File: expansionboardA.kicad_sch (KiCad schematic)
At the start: 52 parts, among them J1 DEBUG, J2 USB_A_Stacked, J3 HDMI_A, J4 FAN, P1 USB_C_Plug, U1 MAX3420EECJ, U2 GPIO_U2, U3 AMS1117-3.3, U4 GPIO_U4, U5 MCP3008T-I/SL, U6 CS4344-CZZR, Y1 Crystal

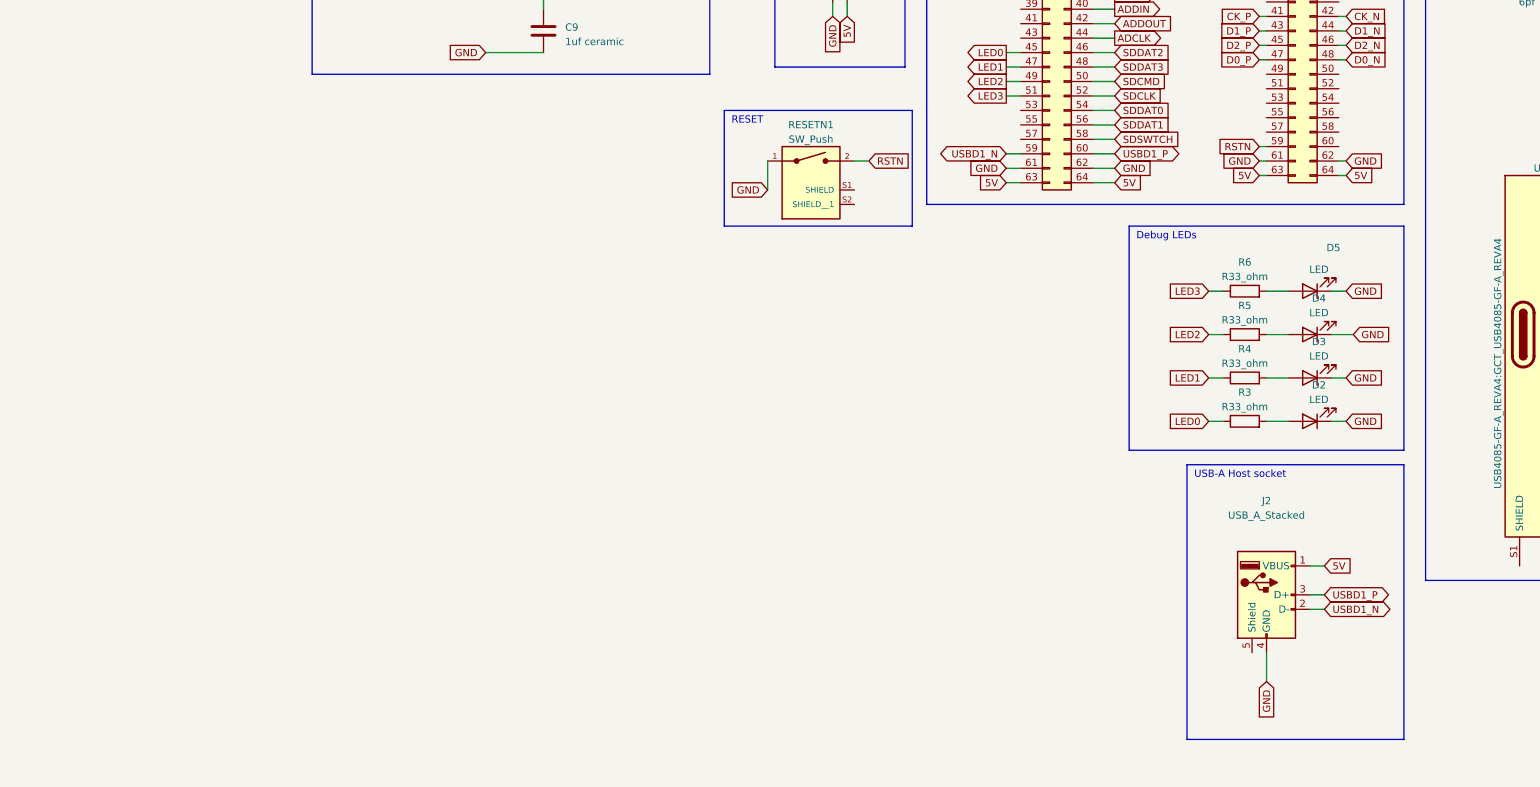
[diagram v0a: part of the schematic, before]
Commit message: Adding USB host chip
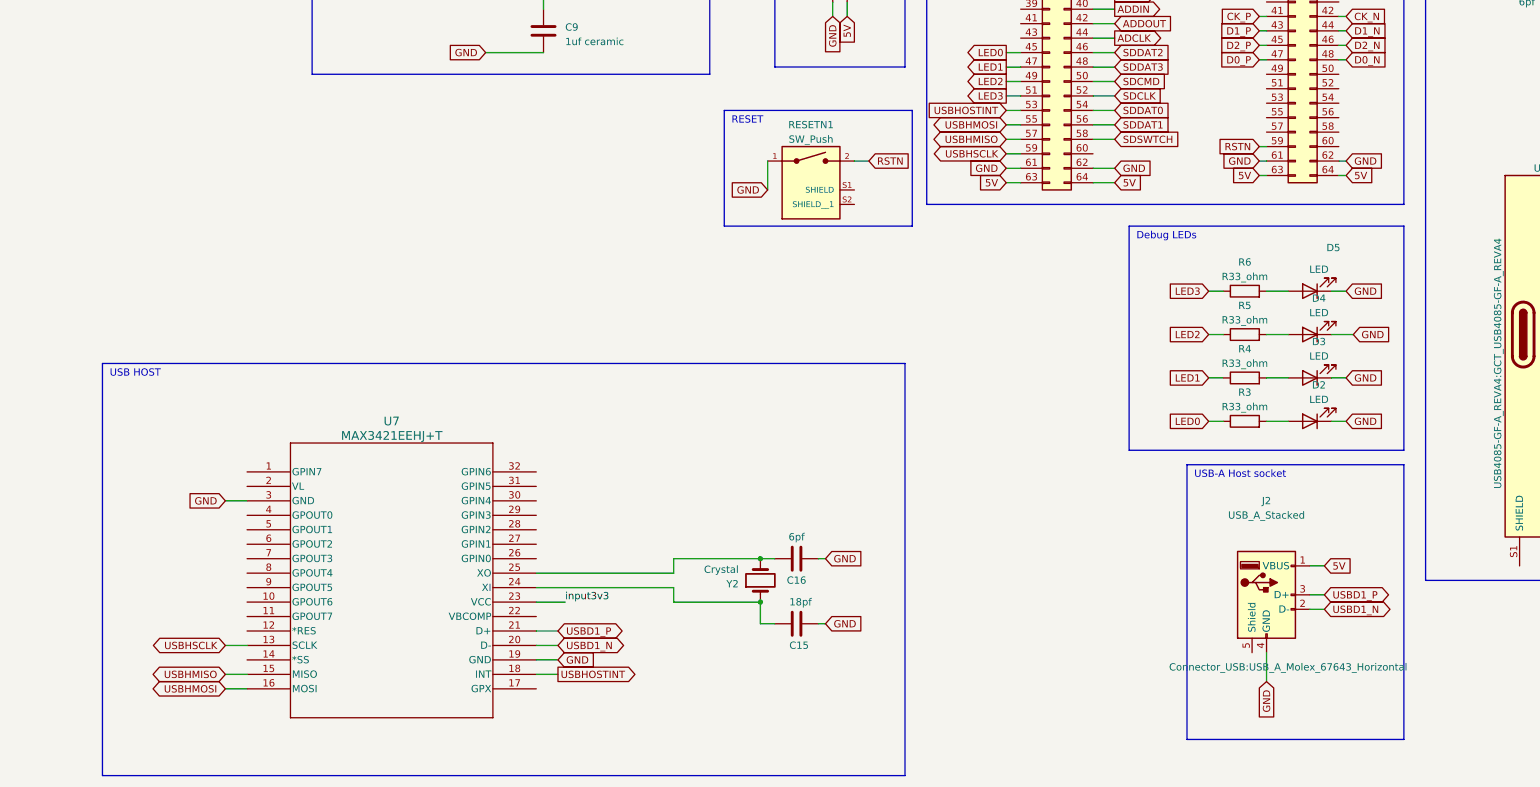
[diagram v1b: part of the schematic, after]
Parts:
- added C15: 18pf, Capacitor_SMD:C_0603_1608Metric_Pad1.08x0.95mm_HandSolder, symbol Device:C
- added C16: 6pf, Capacitor_SMD:C_0603_1608Metric_Pad1.08x0.95mm_HandSolder, symbol Device:C
- added U7: MAX3421EEHJ+T, 21-0110-C_90-0149-32L_MXM, symbol 2023-04-30_01-05-07:MAX3421EEHJ+T
- added Y2: Crystal, Crystal:Crystal_AT310_D3.0mm_L10.0mm_Horizontal, symbol Device:Crystal
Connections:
- net GND: now also C15.1, C16.1, U7.19 (GND), U7.3 (GND)
- net USBD1_N: now also U7.20 (D-); no longer U2.59 (Pin_59)
- net USBD1_P: now also U7.21 (D+); no longer U2.60 (Pin_60)
- net input3v3: now also U7.23 (VCC)
- net USBHOSTINT: now reaches U2.53 (Pin_53)
- net USBHOSTINT: now also U7.18 (INT)
- net USBHMOSI: now reaches U2.55 (Pin_55)
- net USBHMOSI: now also U7.16 (MOSI)
- net USBHMISO: now reaches U2.57 (Pin_57)
- net USBHMISO: now also U7.15 (MISO)
- new net: C15.2, U7.24 (XI), Y2.1
- new net: C16.2, U7.25 (XO), Y2.2
- new net USBHSCLK: U2.59 (Pin_59), U7.13 (SCLK)
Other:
- note added: "USB HOST"

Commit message: Updated board
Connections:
- net USBGPIN0: no longer names the net of U2.21 (Pin_21)
- net USBGPIN0: no longer U1.29 (GPIN0)
- net USBGPIN1: no longer names the net of U2.22 (Pin_22)
- net USBGPIN1: no longer U1.30 (GPIN1)
- net USBGPIN2: no longer names the net of U2.19 (Pin_19)
- net USBGPIN2: no longer U1.31 (GPIN2)
- net USBGPIN3: no longer names the net of U2.20 (Pin_20)
- net USBGPIN3: no longer U1.32 (GPIN3)
- net USBGPOUT0: no longer names the net of U2.17 (Pin_17)
- net USBGPOUT0: no longer U1.1 (GPOUT0)
- net USBGPOUT1: no longer names the net of U2.18 (Pin_18)
- net USBGPOUT1: no longer U1.2 (GPOUT1)
- net USBGPOUT2: no longer names the net of U2.15 (Pin_15)
- net USBGPOUT2: no longer U1.7 (GPOUT2)
- net USBGPOUT3: no longer names the net of U2.16 (Pin_16)
- net USBGPOUT3: no longer U1.8 (GPOUT3)
- net USBHOSTINT renamed USBHINT
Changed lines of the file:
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@@
-    (stroke (width 0) (type default))
-  )
-  (wire (pts (xy 322.58 106.68) (xy 323.85 106.68))
     (stroke (width 0) (type default))
   )
@@
     (stroke (width 0) (type default))
   )
-  (wire (pts (xy 322.58 111.76) (xy 323.85 111.76))
-    (stroke (width 0) (type default))
-  )
   (wire (pts (xy 133.35 109.22) (xy 130.81 109.22))
     (stroke (width 0) (type default))
@@
     (stroke (width 0) (type default))
   )
-  (wire (pts (xy 359.41 106.68) (xy 361.95 106.68))
-    (stroke (width 0) (type default))
-  )
   (wire (pts (xy 378.46 86.36) (xy 378.46 95.25))
     (stroke (width 0) (type default))
@@
     (stroke (width 0) (type default))
   )
-  (wire (pts (xy 322.58 104.14) (xy 323.85 104.14))
-    (stroke (width 0) (type default))
-  )
   (wire (pts (xy 133.35 119.38) (xy 130.81 119.38))
     (stroke (width 0) (type default))
@@
     (stroke (width 0) (type default))
   )
-  (wire (pts (xy 359.41 109.22) (xy 361.95 109.22))
-    (stroke (width 0) (type default))
-  )
   (wire (pts (xy 96.52 25.4) (xy 100.33 25.4))
     (stroke (width 0) (type default))
@@
     (stroke (width 0) (type default))
   )
-  (wire (pts (xy 359.41 104.14) (xy 361.95 104.14))
-    (stroke (width 0) (type default))
-  )
   (wire (pts (xy 379.73 35.56) (xy 387.35 35.56))
     (stroke (width 0) (type default))
@@
     (stroke (width 0) (type default))
   )
-  (wire (pts (xy 359.41 111.76) (xy 361.95 111.76))
-    (stroke (width 0) (type default))
-  )
   (wire (pts (xy 219.71 147.32) (xy 215.9 147.32))
     (stroke (width 0) (type default))
@@
     (stroke (width 0) (type default))
   )
-  (wire (pts (xy 322.58 109.22) (xy 323.85 109.22))
-    (stroke (width 0) (type default))
-  )
   (wire (pts (xy 123.19 109.22) (xy 119.38 109.22))
     (stroke (width 0) (type default))
@@
     (effects (font (size 1.27 1.27)) (justify left bottom))
   )
-  (global_label "USBGPOUT2" (shape input) (at 201.93 96.52 180) (fields_autoplaced)
-    (effects (font (size 1.27 1.27)) (justify right))
-    (property "Intersheetrefs" "${INTERSHEET_REFS}" (at 187.8361 96.52 0)
-      (effects (font (size 1.27 1.27)) (justify right) hide)
-    )
-  )
   (global_label "GND" (shape input) (at 95.25 57.15 180) (fields_autoplaced)
     (effects (font (size 1.27 1.27)) (justify right))
@@
     )
   )
-  (global_label "USBGPOUT0" (shape input) (at 201.93 99.06 180) (fields_autoplaced)
-    (effects (font (size 1.27 1.27)) (justify right))
-    (property "Intersheetrefs" "${INTERSHEET_REFS}" (at 187.8361 99.06 0)
-      (effects (font (size 1.27 1.27)) (justify right) hide)
-    )
-  )
   (global_label "ADCS" (shape output) (at 219.71 124.46 0) (fields_autoplaced)
     (effects (font (size 1.27 1.27)) (justify left))
@@
     )
   )
-  (global_label "USBHOSTINT" (shape input) (at 200.66 144.78 180) (fields_autoplaced)
-    (effects (font (size 1.27 1.27)) (justify right))
-    (property "Intersheetrefs" "${INTERSHEET_REFS}" (at 186.2032 144.78 0)
-      (effects (font (size 1.27 1.27)) (justify right) hide)
-    )
-  )
-  (global_label "USBGPOUT3" (shape output) (at 361.95 111.76 0) (fields_autoplaced)
-    (effects (font (size 1.27 1.27)) (justify left))
-    (property "Intersheetrefs" "${INTERSHEET_REFS}" (at 376.0439 111.76 0)
-      (effects (font (size 1.27 1.27)) (justify left) hide)
-    )
-  )
-  (global_label "USBGPOUT1" (shape output) (at 361.95 106.68 0) (fields_autoplaced)
-    (effects (font (size 1.27 1.27)) (justify left))
-    (property "Intersheetrefs" "${INTERSHEET_REFS}" (at 376.0439 106.68 0)
-      (effects (font (size 1.27 1.27)) (justify left) hide)
+  (global_label "USBHINT" (shape input) (at 200.66 144.78 180) (fields_autoplaced)
+    (effects (font (size 1.27 1.27)) (justify right))
+    (property "Intersheetrefs" "${INTERSHEET_REFS}" (at 189.7108 144.78 0)
+      (effects (font (size 1.27 1.27)) (justify right) hide)
     )
   )
@@
     )
   )
-  (global_label "USBHOSTINT" (shape output) (at 121.92 243.84 0) (fields_autoplaced)
-    (effects (font (size 1.27 1.27)) (justify left))
-    (property "Intersheetrefs" "${INTERSHEET_REFS}" (at 136.3768 243.84 0)
+  (global_label "USBHINT" (shape output) (at 121.92 243.84 0) (fields_autoplaced)
+    (effects (font (size 1.27 1.27)) (justify left))
+    (property "Intersheetrefs" "${INTERSHEET_REFS}" (at 132.8692 243.84 0)
       (effects (font (size 1.27 1.27)) (justify left) hide)
     )
@@
     )
   )
-  (global_label "USBGPIN3" (shape input) (at 322.58 111.76 180) (fields_autoplaced)
-    (effects (font (size 1.27 1.27)) (justify right))
-    (property "Intersheetrefs" "${INTERSHEET_REFS}" (at 310.1794 111.76 0)
-      (effects (font (size 1.27 1.27)) (justify right) hide)
-    )
-  )
   (global_label "D2_P" (shape input) (at 30.48 34.29 180) (fields_autoplaced)
     (effects (font (size 1.27 1.27)) (justify right))
@@
     )
   )
-  (global_label "USBGPOUT3" (shape input) (at 217.17 96.52 0) (fields_autoplaced)
-    (effects (font (size 1.27 1.27)) (justify left))
-    (property "Intersheetrefs" "${INTERSHEET_REFS}" (at 231.2639 96.52 0)
-      (effects (font (size 1.27 1.27)) (justify left) hide)
-    )
-  )
   (global_label "GND" (shape input) (at 287.02 121.92 180) (fields_autoplaced)
     (effects (font (size 1.27 1.27)) (justify right))
@@
     )
   )
-  (global_label "USBGPIN3" (shape output) (at 217.17 101.6 0) (fields_autoplaced)
-    (effects (font (size 1.27 1.27)) (justify left))
-    (property "Intersheetrefs" "${INTERSHEET_REFS}" (at 229.5706 101.6 0)
-      (effects (font (size 1.27 1.27)) (justify left) hide)
-    )
-  )
   (global_label "GND" (shape input) (at 201.93 83.82 180) (fields_autoplaced)
     (effects (font (size 1.27 1.27)) (justify right))
@@
     )
   )
-  (global_label "USBGPIN0" (shape input) (at 322.58 104.14 180) (fields_autoplaced)
-    (effects (font (size 1.27 1.27)) (justify right))
-    (property "Intersheetrefs" "${INTERSHEET_REFS}" (at 310.1794 104.14 0)
-      (effects (font (size 1.27 1.27)) (justify right) hide)
-    )
-  )
   (global_label "USBD1_P" (shape bidirectional) (at 256.54 229.87 0) (fields_autoplaced)
     (effects (font (size 1.27 1.27)) (justify left))
@@
     )
   )
-  (global_label "USBGPIN2" (shape output) (at 200.66 101.6 180) (fields_autoplaced)
-    (effects (font (size 1.27 1.27)) (justify right))
-    (property "Intersheetrefs" "${INTERSHEET_REFS}" (at 188.2594 101.6 0)
-      (effects (font (size 1.27 1.27)) (justify right) hide)
-    )
-  )
   (global_label "ADCH3" (shape input) (at 129.54 83.82 270) (fields_autoplaced)
     (effects (font (size 1.27 1.27)) (justify right))
@@
     )
   )
-  (global_label "USBGPIN2" (shape input) (at 322.58 109.22 180) (fields_autoplaced)
-    (effects (font (size 1.27 1.27)) (justify right))
-    (property "Intersheetrefs" "${INTERSHEET_REFS}" (at 310.1794 109.22 0)
-      (effects (font (size 1.27 1.27)) (justify right) hide)
-    )
-  )
-  (global_label "USBGPIN1" (shape input) (at 322.58 106.68 180) (fields_autoplaced)
-    (effects (font (size 1.27 1.27)) (justify right))
-    (property "Intersheetrefs" "${INTERSHEET_REFS}" (at 310.1794 106.68 0)
-      (effects (font (size 1.27 1.27)) (justify right) hide)
-    )
-  )
-  (global_label "USBGPOUT0" (shape output) (at 361.95 104.14 0) (fields_autoplaced)
-    (effects (font (size 1.27 1.27)) (justify left))
-    (property "Intersheetrefs" "${INTERSHEET_REFS}" (at 376.0439 104.14 0)
-      (effects (font (size 1.27 1.27)) (justify left) hide)
-    )
-  )
   (global_label "GND" (shape input) (at 260.35 82.55 0) (fields_autoplaced)
     (effects (font (size 1.27 1.27)) (justify left))
@@
     )
   )
-  (global_label "USBGPOUT2" (shape output) (at 361.95 109.22 0) (fields_autoplaced)
-    (effects (font (size 1.27 1.27)) (justify left))
-    (property "Intersheetrefs" "${INTERSHEET_REFS}" (at 376.0439 109.22 0)
-      (effects (font (size 1.27 1.27)) (justify left) hide)
-    )
-  )
   (global_label "CK_P" (shape input) (at 30.48 49.53 180) (fields_autoplaced)
     (effects (font (size 1.27 1.27)) (justify right))
@@
     )
   )
-  (global_label "USBGPIN1" (shape output) (at 217.17 104.14 0) (fields_autoplaced)
-    (effects (font (size 1.27 1.27)) (justify left))
-    (property "Intersheetrefs" "${INTERSHEET_REFS}" (at 229.5706 104.14 0)
-      (effects (font (size 1.27 1.27)) (justify left) hide)
-    )
-  )
   (global_label "GND" (shape input) (at 177.8 53.34 180) (fields_autoplaced)
     (effects (font (size 1.27 1.27)) (justify right))
@@
     )
   )
-  (global_label "USBGPIN0" (shape output) (at 200.66 104.14 180) (fields_autoplaced)
-    (effects (font (size 1.27 1.27)) (justify right))
-    (property "Intersheetrefs" "${INTERSHEET_REFS}" (at 188.2594 104.14 0)
-      (effects (font (size 1.27 1.27)) (justify right) hide)
-    )
-  )
   (global_label "SDDAT0" (shape input) (at 177.8 27.94 180) (fields_autoplaced)
     (effects (font (size 1.27 1.27)) (justify right))
@@
     )
   )
-  (global_label "USBGPX" (shape input) (at 361.95 91.44 0) (fields_autoplaced)
+  (global_label "USBGPX" (shape output) (at 361.95 91.44 0) (fields_autoplaced)
     (effects (font (size 1.27 1.27)) (justify left))
     (property "Intersheetrefs" "${INTERSHEET_REFS}" (at 372.4153 91.44 0)
@@
     )
   )
-  (global_label "USBGPOUT1" (shape input) (at 217.17 99.06 0) (fields_autoplaced)
-    (effects (font (size 1.27 1.27)) (justify left))
-    (property "Intersheetrefs" "${INTERSHEET_REFS}" (at 231.2639 99.06 0)
-      (effects (font (size 1.27 1.27)) (justify left) hide)
-    )
-  )

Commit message: Fixed some errors on the board
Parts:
- added R15: 10_kohm, Resistor_SMD:R_0603_1608Metric_Pad0.98x0.95mm_HandSolder, symbol Device:R
- C4: value 6pf -> 18pf
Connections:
- net INT: now also R15.1
- net input3v3: now also R15.2
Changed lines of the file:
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@@
   (junction (at 359.41 57.15) (diameter 0) (color 0 0 0 0)
   )
+  (junction (at 375.92 86.36) (diameter 0) (color 0 0 0 0)
+  )
   (junction (at 241.3 39.37) (diameter 0) (color 0 0 0 0)
   )
@@
   (junction (at 119.38 119.38) (diameter 0) (color 0 0 0 0)
   )
+  (junction (at 360.68 93.98) (diameter 0) (color 0 0 0 0)
+  )
   (junction (at 307.34 96.52) (diameter 0) (color 0 0 0 0)
   )
@@
     (stroke (width 0) (type default))
   )
+  (wire (pts (xy 360.68 93.98) (xy 361.95 93.98))
+    (stroke (width 0) (type default))
+  )
   (wire (pts (xy 171.45 25.4) (xy 182.88 25.4))
     (stroke (width 0) (type default))
@@
     (stroke (width 0) (type default))
   )
-  (wire (pts (xy 361.95 86.36) (xy 378.46 86.36))
+  (wire (pts (xy 375.92 101.6) (xy 375.92 86.36))
+    (stroke (width 0) (type default))
+  )
+  (wire (pts (xy 361.95 86.36) (xy 375.92 86.36))
     (stroke (width 0) (type default))
   )
@@
     (stroke (width 0) (type default))
   )
-  (wire (pts (xy 359.41 93.98) (xy 361.95 93.98))
+  (wire (pts (xy 359.41 93.98) (xy 360.68 93.98))
     (stroke (width 0) (type default))
   )
@@
     (stroke (width 0) (type default))
   )
+  (wire (pts (xy 360.68 93.98) (xy 360.68 101.6))
+    (stroke (width 0) (type default))
+  )
   (wire (pts (xy 246.38 130.81) (xy 245.11 130.81))
     (stroke (width 0) (type default))
@@
     (stroke (width 0) (type default))
   )
+  (wire (pts (xy 360.68 101.6) (xy 363.22 101.6))
+    (stroke (width 0) (type default))
+  )
   (wire (pts (xy 219.71 127) (xy 215.9 127))
     (stroke (width 0) (type default))
@@
     (stroke (width 0) (type default))
   )
+  (wire (pts (xy 370.84 101.6) (xy 375.92 101.6))
+    (stroke (width 0) (type default))
+  )
   (wire (pts (xy 302.26 224.79) (xy 298.45 224.79))
     (stroke (width 0) (type default))
@@
     (stroke (width 0) (type default))
   )
+  (wire (pts (xy 375.92 86.36) (xy 378.46 86.36))
+    (stroke (width 0) (type default))
+  )
   (wire (pts (xy 287.02 121.92) (xy 288.29 121.92))
     (stroke (width 0) (type default))
@@
     )
   )
+  (symbol (lib_id "Device:R") (at 367.03 101.6 90) (unit 1)
+    (in_bom yes) (on_board yes) (dnp no) (fields_autoplaced)
+    (property "Reference" "R15" (at 367.03 96.52 90)
+      (effects (font (size 1.27 1.27)))
+    )
+    (property "Value" "10_kohm" (at 367.03 99.06 90)
+      (effects (font (size 1.27 1.27)))
+    )
+    (property "Footprint" "Resistor_SMD:R_0603_1608Metric_Pad0.98x0.95mm_HandSolder" (at 367.03 103.378 90)
+      (effects (font (size 1.27 1.27)) hide)
+    )
+    (property "Datasheet" "~" (at 367.03 101.6 0)
+      (effects (font (size 1.27 1.27)) hide)
+    )
+    (pin "1")
+    (pin "2")
+    (instances
+      (project "expansionboardA"
+        (path "/317f7f3e-4535-46d0-9a87-af1bea12706a"
+          (reference "R15") (unit 1)
+        )
+      )
+    )
+  )
   (symbol (lib_id "Connector_Generic:Conn_01x02") (at 170.18 120.65 90) (unit 1)
     (in_bom yes) (on_board yes) (dnp no)
@@
       (effects (font (size 1.27 1.27)))
     )
-    (property "Value" "6pf" (at 292.1 125.73 90)
+    (property "Value" "18pf" (at 292.1 125.73 90)
       (effects (font (size 1.27 1.27)))
     )

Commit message: Updated board
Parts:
- removed R15: 10_kohm, Resistor_SMD:R_0603_1608Metric_Pad0.98x0.95mm_HandSolder, symbol Device:R
- added C17: 1uf ceramic, Capacitor_SMD:C_0603_1608Metric_Pad1.08x0.95mm_HandSolder, symbol Device:C
- added C18: 0.1uf, Capacitor_SMD:C_0603_1608Metric_Pad1.08x0.95mm_HandSolder, symbol Device:C
- added C20: 4.7uf, Capacitor_THT:CP_Radial_D4.0mm_P1.50mm, symbol Device:C_Polarized_Small_US
- added R16, R17: R33_ohm, Resistor_SMD:R_0603_1608Metric_Pad0.98x0.95mm_HandSolder, symbol Device:R
- added R18: 10_kohm, Resistor_SMD:R_0603_1608Metric_Pad0.98x0.95mm_HandSolder, symbol Device:R
- C16: value 6pf -> 18pf
- C5: value 1uf ceramic -> 4.7uf; footprint Capacitor_SMD:C_0603_1608Metric_Pad1.08x0.95mm_HandSolder -> Capacitor_THT:CP_Radial_D4.0mm_P1.50mm; symbol Device:C -> Device:C_Polarized_Small_US
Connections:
- net 5V: now also C20.1
- net GND: now also C5.2, J2.5 (Shield), C17.1, C18.1, C20.2; no longer C5.1
- net LED0: now also U2.43 (Pin_43); no longer U2.45 (Pin_45)
- net LED1: now also U2.45 (Pin_45); no longer U2.47 (Pin_47)
- net LED2: now also U2.47 (Pin_47); no longer U2.49 (Pin_49)
- net LED3: now also U2.49 (Pin_49); no longer U2.51 (Pin_51)
- net USBCBUSPOWER: now also C5.1; no longer C5.2
- net USBD1_N: now also R17.2; no longer J2.2 (D-)
- net USBD1_P: now also R16.2; no longer J2.3 (D+)
- net input3v3: now also U7.2 (VL), C17.2, C18.2, R18.2
- net USBHRES: now reaches U7.12 (*RES)
- net USBHRES: now also U2.51 (Pin_51)
- net USBHCSN: now reaches U7.14 (*SS)
- net USBHCSN: now also U2.60 (Pin_60)
- net USBHGPX: now reaches U7.17 (GPX)
- net GPIH: now reaches U7.22 (VBCOMP)
- net GPIH: now also R18.1
- new net: J2.2 (D-), R17.1
- new net: J2.3 (D+), R16.1
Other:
- note removed: "USB-A Host socket"
- moved on the sheet: C15, C16, J2, Y2

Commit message: Updated board
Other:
- note added: "Debug Port"
- note added: "Status LEDs"
- note removed: "Debug LEDs"
- note removed: "Serial Debug Port"
- company: (none) -> Engin Cilasun
- title: (none) -> Expansion Board A
- moved on the sheet: ADC1, AU1, C1, C10, C11, C12, C13, C14, C15, C16, C17, C18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
